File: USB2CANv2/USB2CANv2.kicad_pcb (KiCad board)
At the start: 4 copper layers, 46.1 x 20.3 mm, 66 parts, among them IC1 MIC5528-3.3YMT-TR, J1 USB_C_Receptacle_USB2.0, J2 Conn_01x06_Pin, J3 Conn_01x02_Pin, J4 Conn_01x02_Pin, J5 Conn_01x02_Pin, SW1 SW_BOOT0, U1 STM32F405RGTx, U2 USBLC6-2P6, U3 MCP2561-E-SN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

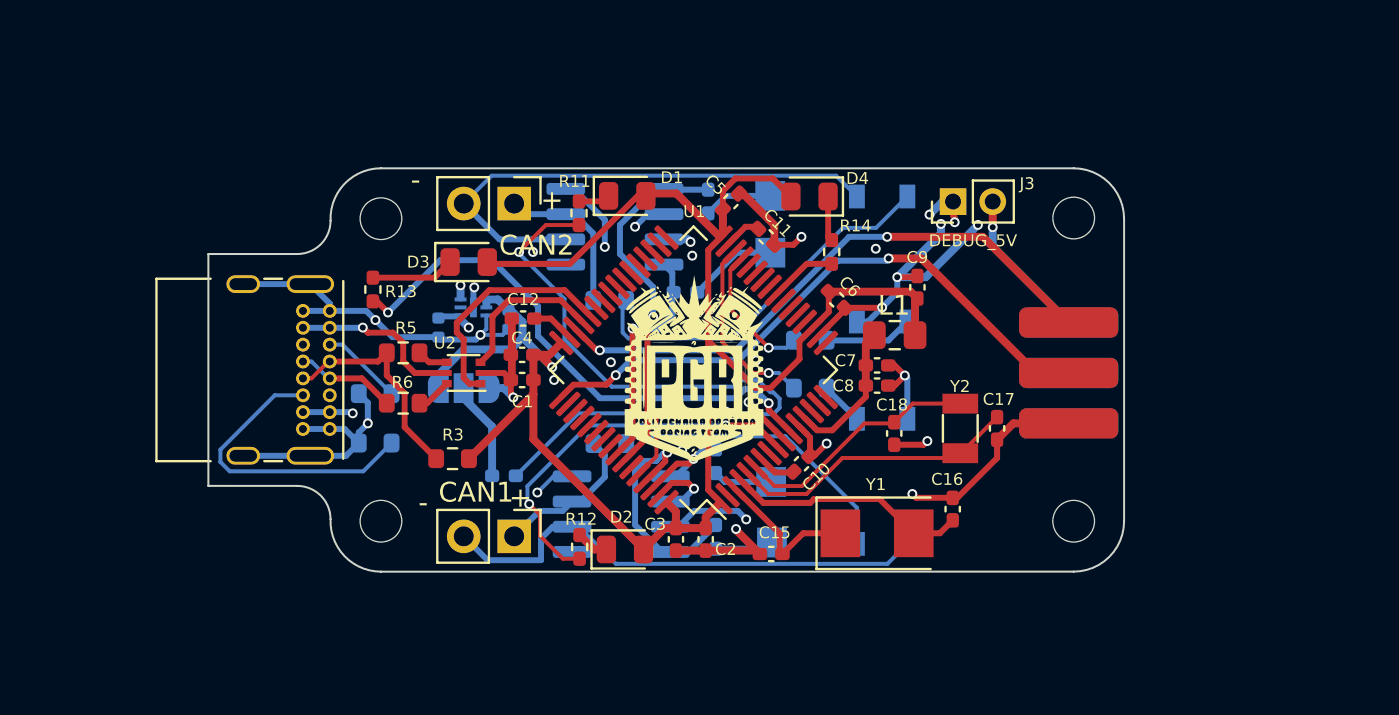
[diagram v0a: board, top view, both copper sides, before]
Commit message: Changed stack-up, Silkscreen improvments + LSE HSE SWAP
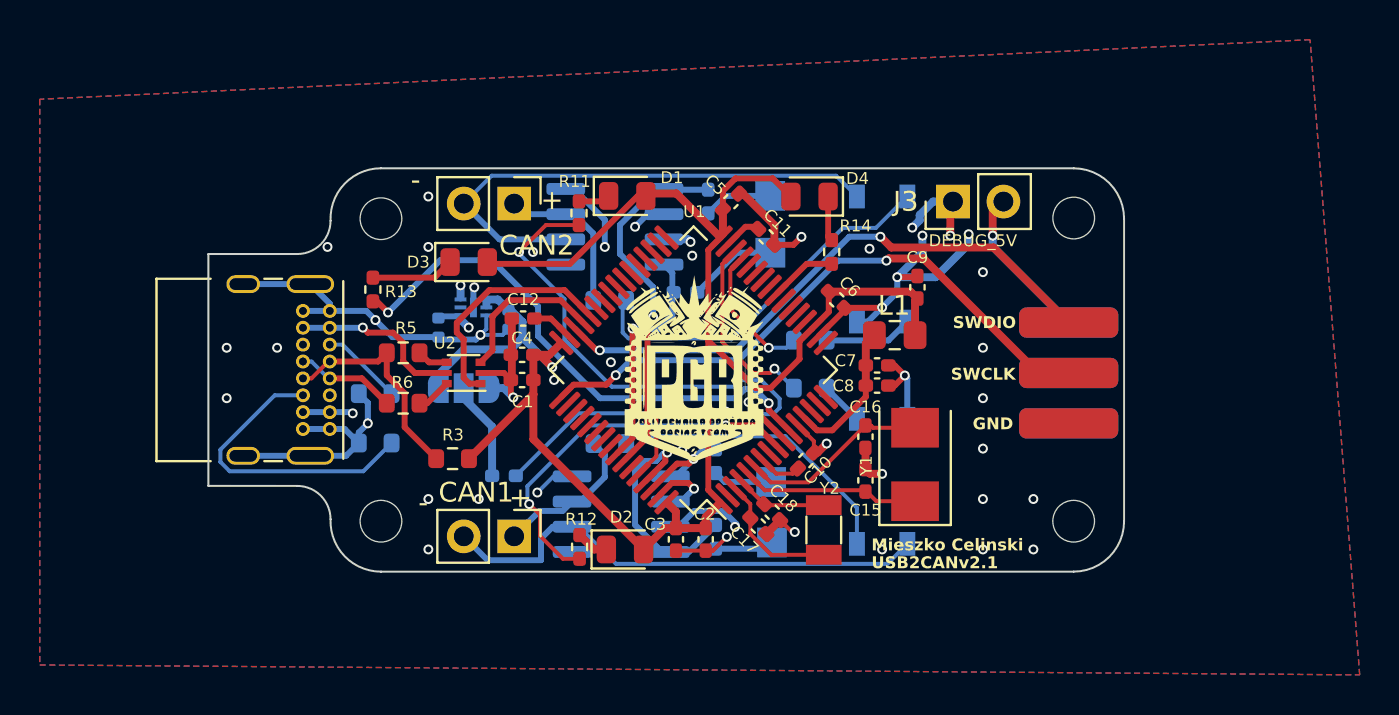
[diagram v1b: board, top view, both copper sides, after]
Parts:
- J3: footprint Connector_PinHeader_2.00mm:PinHeader_1x02_P2.00mm_Vertical -> Connector_PinHeader_2.54mm:PinHeader_1x02_P2.54mm_Vertical
- Y1: value 16MHz -> ABM3-16.000MHZ-B4Y-T
- moved C17 13.0 mm to (148.7, 105.5), turned to -45 degrees
- moved Y2 8.57 mm to (152.0, 105.7)
- moved C18 7.32 mm to (149.4, 104.8), turned to -45 degrees
- moved C15 6.02 mm to (154.1, 103.2), turned to 90 degrees
- moved C16 5.71 mm to (154.1, 101.0), turned to -90 degrees
- moved Y1 3.96 mm to (156.6, 102.4), turned to 90 degrees
- moved C10 0.28 mm to (151.1, 102.2)
- turned G*** to 180 degrees
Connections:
- C15 pad 1: /LSE_IN -> /HSE_IN
- C16 pad 1: /LSE_OUT -> /HSE_OUT
- C17 pad 1: /HSE_IN -> /LSE_IN
- C18 pad 1: /HSE_OUT -> /LSE_OUT
- Y1 pad 1: /LSE_IN -> /HSE_IN
- Y1 pad 2: /LSE_OUT -> /HSE_OUT
- Y2 pad 1: /HSE_IN -> /LSE_IN
- Y2 pad 2: /HSE_OUT -> /LSE_OUT
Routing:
- net GND: track 96.2 -> 83.5 mm, vias 30 -> 47
- net /LSE_OUT: track 12.2 -> 4.65 mm
- net /HSE_IN: track 14.5 -> 8.95 mm
- net /HSE_OUT: track 12.4 -> 9.58 mm
- net +5V: track 22.4 -> 24.1 mm
- net /DEBUG_5V: track 8.98 -> 7.68 mm
- net /LSE_IN: track 7.66 -> 6.77 mm
- added copper zone on B.Cu, net GND
- added copper zone on F.Cu, net GND
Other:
- board text added: "DEBUG 5V"
- board text added: "GND"
- board text added: "Mieszko Celinski"
- board text added: "SWCLK"
- board text added: "SWDIO"
- board text added: "USB2CANv2.1"
- board text removed: "Mieszko Celinski Karol Pergol"
- board text removed: "USB2CANv2"
